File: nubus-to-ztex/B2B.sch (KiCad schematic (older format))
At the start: 17 parts, among them J1 Conn_02x07_Odd_Even, J3 Conn_01x06_Male

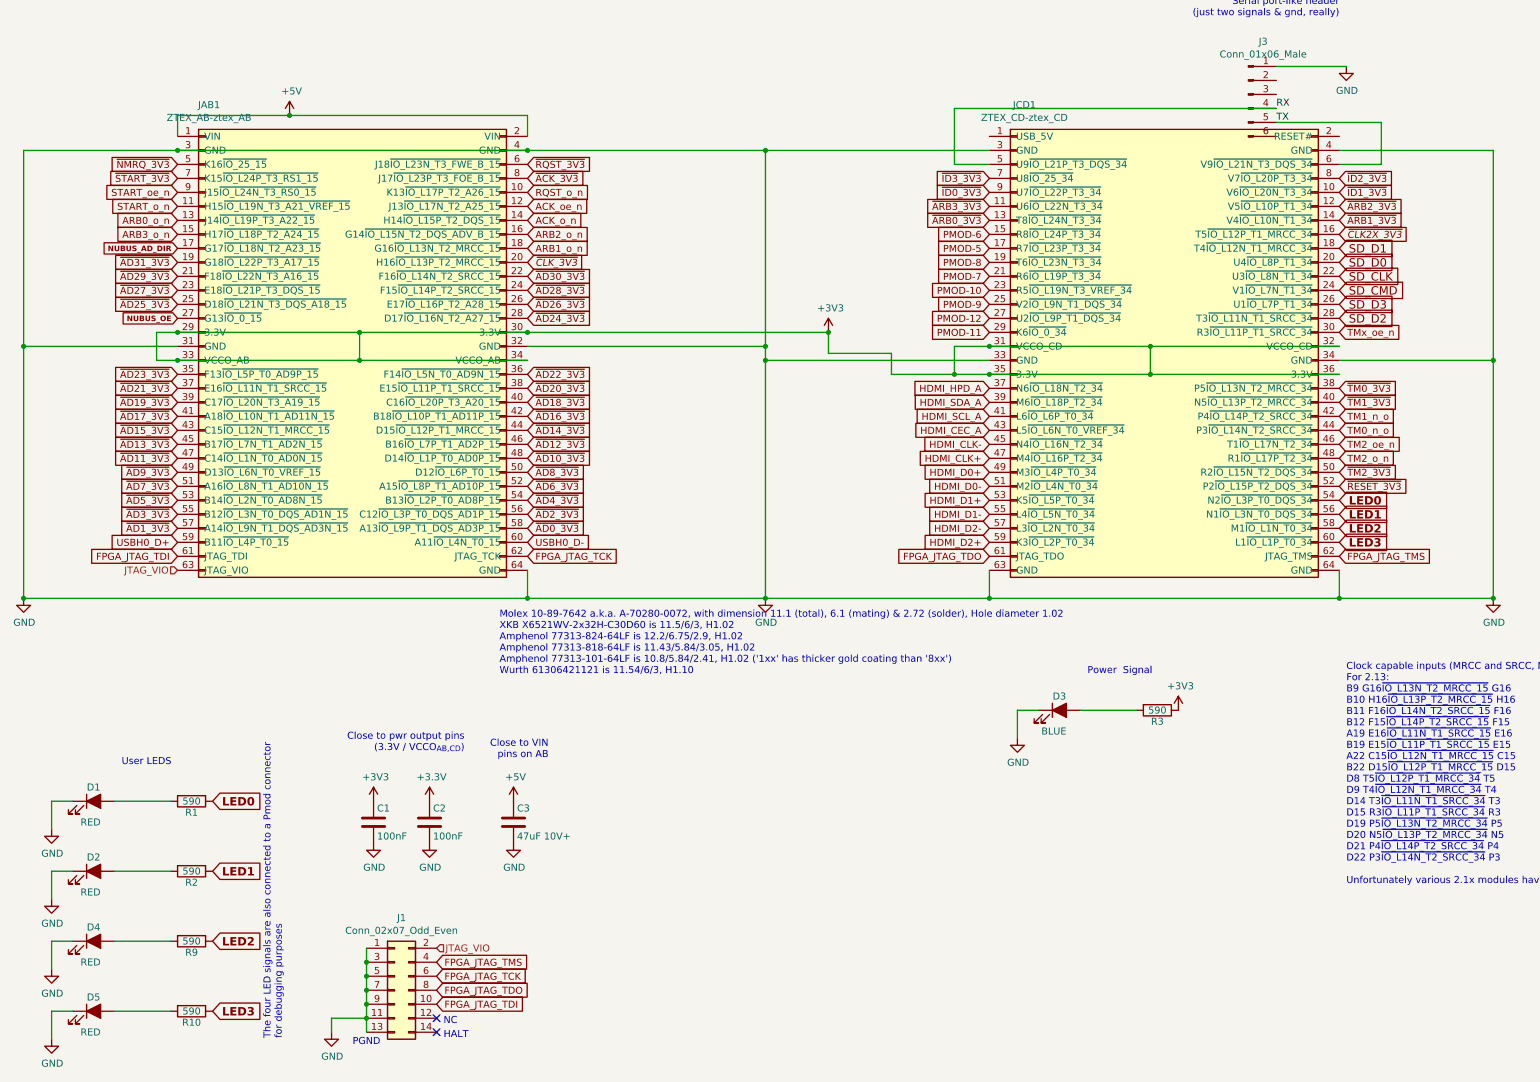
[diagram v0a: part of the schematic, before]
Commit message: merge pmod & leds into an extended pmod on the outside. Also some BoM updates.
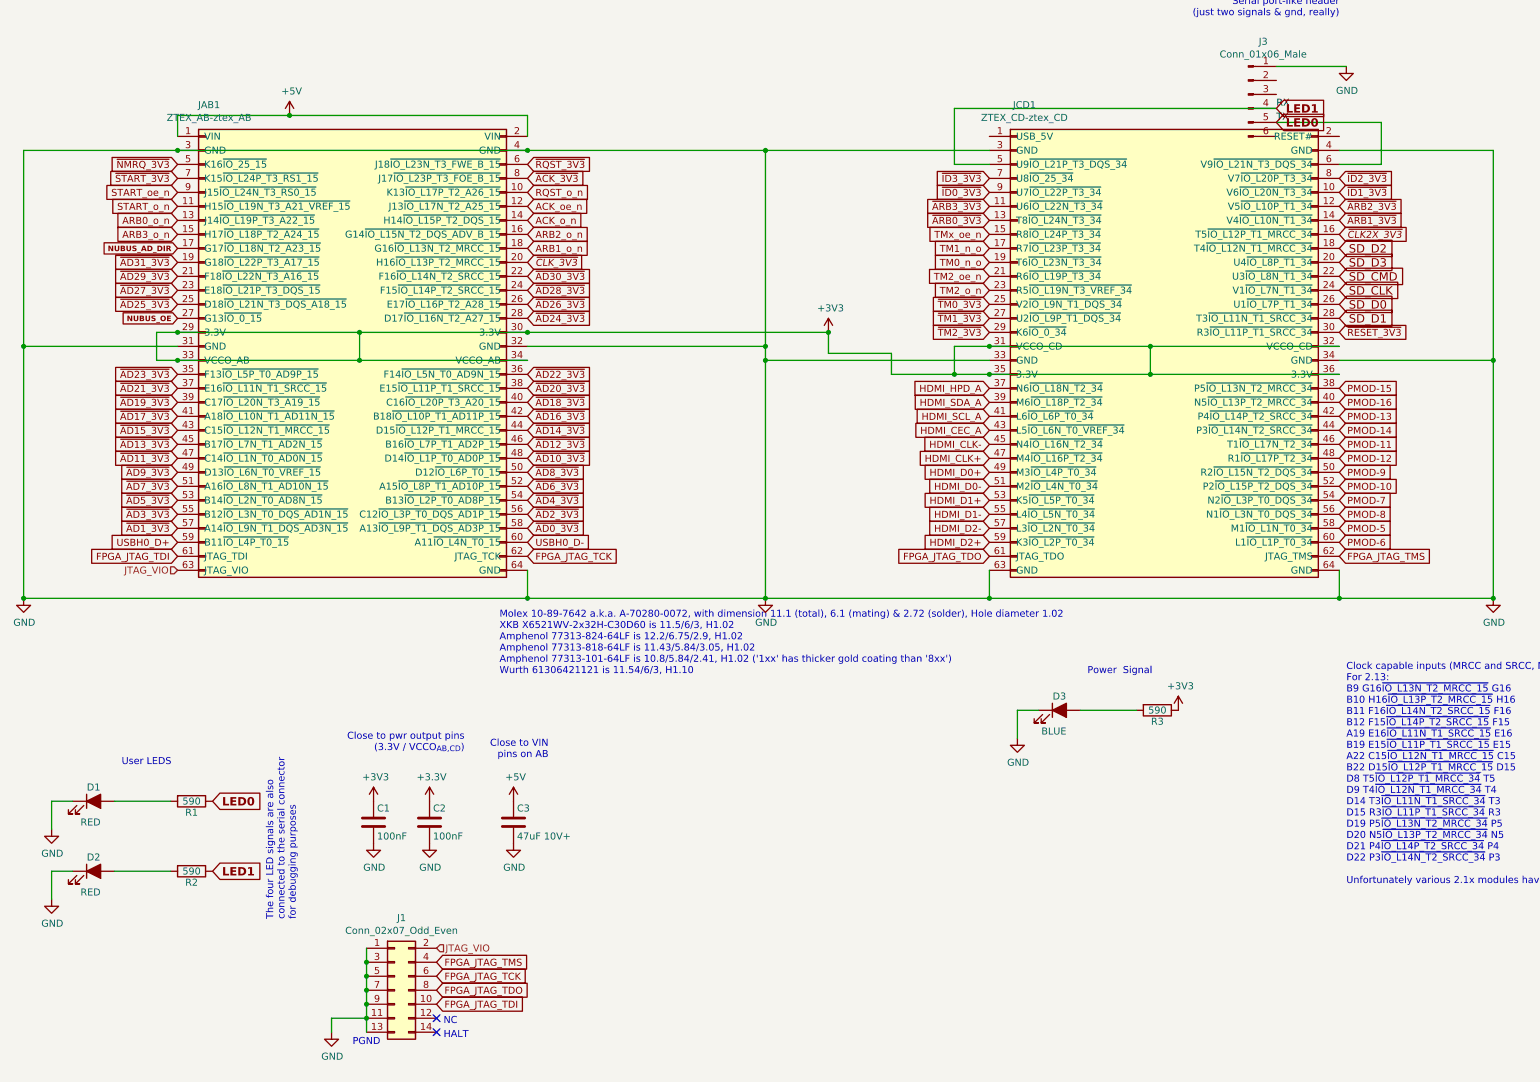
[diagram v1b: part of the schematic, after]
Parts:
- removed D4, D5: RED, LED_SMD:LED_0805_2012Metric, symbol Device:LED_ALT
- removed R10, R9: 590, Resistor_SMD:R_0603_1608Metric, symbol Device:R
- C2: URL (none) -> https://lcsc.com/product-detail/Multilayer-Ceramic-Capacito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
- C3: MPN C2012X5R1A476MTJ00E -> GRM21BR61A476ME15K; MPN-ALT (none) -> C2012X5R1A476MTJ00E; URL https://lcsc.com/product-detail/Multilayer-Ceramic-Capacito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 -> https://www.lcsc.com/product-detail/Multilayer-Ceramic-Capa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; URL-ALT (none) -> https://lcsc.com/product-detail/Multilayer-Ceramic-Capacito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
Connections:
- net LED2 is gone; now on net PMOD-5: JCD1.58 (M1~IO_L1N_T0_34)
- net LED3 is gone; now on net PMOD-6: JCD1.60 (L1~IO_L1P_T0_34)
- net RX is gone; now on net LED1: J3.4 (Pin_4), JCD1.5 (U9~IO_L21P_T3_DQS_34)
- net TX is gone; now on net LED0: J3.5 (Pin_5), JCD1.6 (V9~IO_L21N_T3_DQS_34)
- net LED0: no longer JCD1.54 (N2~IO_L3P_T0_DQS_34)
- net LED1: no longer JCD1.56 (N1~IO_L3N_T0_DQS_34)
- net PMOD-10: now also JCD1.52 (P2~IO_L15P_T2_DQS_34); no longer JCD1.23 (R5~IO_L19N_T3_VREF_34)
- net PMOD-11: now also JCD1.46 (T1~IO_L17N_T2_34); no longer JCD1.29 (K6~IO_0_34)
- net PMOD-12: now also JCD1.48 (R1~IO_L17P_T2_34); no longer JCD1.27 (U2~IO_L9P_T1_DQS_34)
- net PMOD-5: no longer JCD1.17 (R7~IO_L23P_T3_34)
- net PMOD-6: no longer JCD1.15 (R8~IO_L24P_T3_34)
- net PMOD-7: now also JCD1.54 (N2~IO_L3P_T0_DQS_34); no longer JCD1.21 (R6~IO_L19P_T3_34)
- net PMOD-8: now also JCD1.56 (N1~IO_L3N_T0_DQS_34); no longer JCD1.19 (T6~IO_L23N_T3_34)
- net PMOD-9: now also JCD1.50 (R2~IO_L15N_T2_DQS_34); no longer JCD1.25 (V2~IO_L9N_T1_DQS_34)
- net SD_CLK: now also JCD1.24 (V1~IO_L7N_T1_34); no longer JCD1.22 (U3~IO_L8N_T1_34)
- net SD_CMD: now also JCD1.22 (U3~IO_L8N_T1_34); no longer JCD1.24 (V1~IO_L7N_T1_34)
- net SD_D0: now also JCD1.26 (U1~IO_L7P_T1_34); no longer JCD1.20 (U4~IO_L8P_T1_34)
- net SD_D1: now also JCD1.28 (T3~IO_L11N_T1_SRCC_34); no longer JCD1.18 (T4~IO_L12N_T1_MRCC_34)
- net SD_D2: now also JCD1.18 (T4~IO_L12N_T1_MRCC_34); no longer JCD1.28 (T3~IO_L11N_T1_SRCC_34)
- net SD_D3: now also JCD1.20 (U4~IO_L8P_T1_34); no longer JCD1.26 (U1~IO_L7P_T1_34)
- net TM0_n_o: now also JCD1.19 (T6~IO_L23N_T3_34); no longer JCD1.44 (P3~IO_L14N_T2_SRCC_34)
- net TM1_n_o: now also JCD1.17 (R7~IO_L23P_T3_34); no longer JCD1.42 (P4~IO_L14P_T2_SRCC_34)
- net TM2_o_n: now also JCD1.23 (R5~IO_L19N_T3_VREF_34); no longer JCD1.48 (R1~IO_L17P_T2_34)
- net TM2_oe_n: now also JCD1.21 (R6~IO_L19P_T3_34); no longer JCD1.46 (T1~IO_L17N_T2_34)
- net TMx_oe_n: now also JCD1.15 (R8~IO_L24P_T3_34); no longer JCD1.30 (R3~IO_L11P_T1_SRCC_34)
- net ~RESET_3V3: now also JCD1.30 (R3~IO_L11P_T1_SRCC_34); no longer JCD1.52 (P2~IO_L15P_T2_DQS_34)
- net ~TM0_3V3: now also JCD1.25 (V2~IO_L9N_T1_DQS_34); no longer JCD1.38 (P5~IO_L13N_T2_MRCC_34)
- net ~TM1_3V3: now also JCD1.27 (U2~IO_L9P_T1_DQS_34); no longer JCD1.40 (N5~IO_L13P_T2_MRCC_34)
- net ~TM2_3V3: now also JCD1.29 (K6~IO_0_34); no longer JCD1.50 (R2~IO_L15N_T2_DQS_34)
- new net PMOD-13: JCD1.42 (P4~IO_L14P_T2_SRCC_34)
- new net PMOD-14: JCD1.44 (P3~IO_L14N_T2_SRCC_34)
- new net PMOD-15: JCD1.38 (P5~IO_L13N_T2_MRCC_34)
- new net PMOD-16: JCD1.40 (N5~IO_L13P_T2_MRCC_34)
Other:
- note added: "The four LED signals are also\nconnected to the serial connector\nfor debugging purposes"
- note removed: "The four LED signals are also connected to a Pmod connector\nfor debugging purposes"
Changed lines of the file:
@@
 $Descr A4 11693 8268
 encoding utf-8
-Sheet 2 10
+Sheet 2 9
 Title "nubus-to-ztex B2B connector"
 Date ""
@@
 	1    0    0    -1
 $EndComp
-Connection ~ 6250 2550
 Wire Wire Line
 	11000 2750 11000 4450
@@
 Text GLabel 4100 2150 2    50   Input ~ 0
 ~AD30_3V3
-Text GLabel 9900 3650 2    50   Input ~ 0
+Text GLabel 9900 2550 2    50   Input ~ 0
 ~RESET_3V3
-Text GLabel 9900 3050 2    50   Input ~ 0
+Text GLabel 7400 2450 0    50   Input ~ 0
 ~TM1_3V3
-Text GLabel 9900 2950 2    50   Input ~ 0
+Text GLabel 7400 2350 0    50   Input ~ 0
 ~TM0_3V3
 Text GLabel 1600 3950 0    50   Input ~ 0
@@
 Text GLabel 1850 6400 2    60   Input ~ 12
 LED1
-Text GLabel 9900 3750 2    60   Input ~ 12
+Text GLabel 9450 1050 2    60   Input ~ 12
 LED0
-Text GLabel 9900 3850 2    60   Input ~ 12
+Text GLabel 9450 950  2    60   Input ~ 12
 LED1
 Text GLabel 1600 4050 0    50   Input ~ 0
@@
 F 9 "?" H 3400 6050 50  0001 C CNN "Koncar"
 F 10 "TB" H 3400 6050 50  0001 C CNN "Side"
+F 11 "https://lcsc.com/product-detail/Multilayer-Ceramic-Capacitors-MLCC-SMD-SMT_YAGEO-CC0603KRX7R8BB104_C92490.html" H 3400 6050 50  0001 C CNN "URL"
 	1    3400 6050
 	1    0    0    -1
@@
 Text GLabel 1600 1350 0    50   Input ~ 0
 ~NMRQ_3V3
-Text GLabel 9900 3550 2    50   Input ~ 0
+Text GLabel 7400 2550 0    50   Input ~ 0
 ~TM2_3V3
 Text GLabel 9900 1850 2    50   Input Italic 0
@@
 F 2 "Capacitor_SMD:C_0805_2012Metric" H 4038 5900 50  0001 C CNN
 F 3 "" H 4000 6050 50  0000 C CNN
-F 4 "C2012X5R1A476MTJ00E" H 4000 6050 50  0001 C CNN "MPN"
-F 5 "https://lcsc.com/product-detail/Multilayer-Ceramic-Capacitors-MLCC-SMD-SMT_TDK-C2012X5R1A476MTJ00E_C76636.html" H 4000 6050 50  0001 C CNN "URL"
+F 4 "C2012X5R1A476MTJ00E" H 4000 6050 50  0001 C CNN "MPN-ALT"
+F 5 "https://lcsc.com/product-detail/Multilayer-Ceramic-Capacitors-MLCC-SMD-SMT_TDK-C2012X5R1A476MTJ00E_C76636.html" H 4000 6050 50  0001 C CNN "URL-ALT"
+F 6 "GRM21BR61A476ME15K" H 4000 6050 50  0001 C CNN "MPN"
+F 7 "https://www.lcsc.com/product-detail/Multilayer-Ceramic-Capacitors-MLCC-SMD-SMT_Murata-Electronics-GRM21BR61A476ME15K_C2292827.html" H 4000 6050 50  0001 C CNN "URL"
 	1    4000 6050
 	1    0    0    -1
@@
 Text GLabel 1600 1550 0    50   Input ~ 0
 START_oe_n
-Text GLabel 9900 2550 2    50   Input ~ 0
+Text GLabel 7400 1850 0    50   Input ~ 0
 TMx_oe_n
-Text GLabel 9900 3150 2    50   Input ~ 0
+Text GLabel 7400 1950 0    50   Input ~ 0
 TM1_n_o
-Text GLabel 9900 3250 2    50   Input ~ 0
+Text GLabel 7400 2050 0    50   Input ~ 0
 TM0_n_o
+Text GLabel 7400 2150 0    50   Input ~ 0
+TM2_oe_n
+Text GLabel 7400 2250 0    50   Input ~ 0
+TM2_o_n
+Text GLabel 9900 1950 2    60   Input ~ 0
+SD_D2
+Text GLabel 9900 2050 2    60   Input ~ 0
+SD_D3
+Text GLabel 9900 2150 2    60   Input ~ 0
+SD_CMD
+Text GLabel 9900 2250 2    60   Input ~ 0
+SD_CLK
+Text GLabel 9900 2350 2    60   Input ~ 0
+SD_D0
+Text GLabel 9900 2450 2    60   Input ~ 0
+SD_D1
+Text GLabel 9900 3950 2    50   Input ~ 0
+PMOD-5
+Text GLabel 9900 3750 2    50   Input ~ 0
+PMOD-7
+Text GLabel 9900 3550 2    50   Input ~ 0
+PMOD-9
 Text GLabel 9900 3350 2    50   Input ~ 0
-TM2_oe_n
+PMOD-11
 Text GLabel 9900 3450 2    50   Input ~ 0
-TM2_o_n
-Text GLabel 9900 2450 2    60   Input ~ 0
-SD_D2
-Text GLabel 9900 2350 2    60   Input ~ 0
-SD_D3
-Text GLabel 9900 2250 2    60   Input ~ 0
-SD_CMD
-Text GLabel 9900 2150 2    60   Input ~ 0
-SD_CLK
-Text GLabel 9900 2050 2    60   Input ~ 0
-SD_D0
-Text GLabel 9900 1950 2    60   Input ~ 0
-SD_D1
-Text GLabel 7400 1950 0    50   Input ~ 0
-PMOD-5
-Text GLabel 7400 2150 0    50   Input ~ 0
-PMOD-7
-Text GLabel 7400 2350 0    50   Input ~ 0
-PMOD-9
-Text GLabel 7400 2550 0    50   Input ~ 0
-PMOD-11
-Text GLabel 7400 2450 0    50   Input ~ 0
 PMOD-12
-Text GLabel 7400 1850 0    50   Input ~ 0
+Text GLabel 9900 4050 2    50   Input ~ 0
 PMOD-6
-Text GLabel 7400 2050 0    50   Input ~ 0
+Text GLabel 9900 3850 2    50   Input ~ 0
 PMOD-8
-Text GLabel 7400 2250 0    50   Input ~ 0
+Text GLabel 9900 3650 2    50   Input ~ 0
 PMOD-10
-Wire Wire Line
-	850  6900 700  6900
-Wire Wire Line
-	700  6900 700  7100
-Wire Wire Line
-	1150 6900 1550 6900
-$Comp
-L Device:R R?
-U 1 1 62CD698B
-P 1700 6900
-AR Path="/5F6B165A/62CD698B" Ref="R?"  Part="1"
-AR Path="/5F67E4B9/62CD698B" Ref="R?"  Part="1"
-AR Path="/618E8C75/62CD698B" Ref="R9"  Part="1"
-F 0 "R9" V 1780 6900 50  0000 C CNN
-F 1 "590" V 1700 6900 50  0000 C CNN
-F 2 "Resistor_SMD:R_0603_1608Metric" V 1630 6900 50  0001 C CNN
-F 3 "" H 1700 6900 50  0000 C CNN
-F 4 "0603WAF5900T5E" V 1700 6900 50  0001 C CNN "MPN"
-F 5 "https://www.lcsc.com/product-detail/Chip-Resistor-Surface-Mount_UNI-ROYAL-Uniroyal-Elec-0603WAF5900T5E_C23084.html" V 1700 6900 50  0001 C CNN "URL"
-	1    1700 6900
-	0    1    1    0
-$EndComp
-$Comp
-L Device:LED_ALT D?
-U 1 1 62CD6995
-P 1000 6900
-AR Path="/5F6B165A/62CD6995" Ref="D?"  Part="1"
-AR Path="/5F67E4B9/62CD6995" Ref="D?"  Part="1"
-AR Path="/618E8C75/62CD6995" Ref="D4"  Part="1"
-F 0 "D4" H 1000 7000 50  0000 C CNN
-F 1 "RED" H 1050 6750 50  0000 R CNN
-F 2 "LED_SMD:LED_0805_2012Metric" H 1000 6900 50  0001 C CNN
-F 3 "https://optoelectronics.liteon.com/upload/download/DS-22-99-0150/LTST-C170KRKT.pdf" H 1000 6900 50  0001 C CNN
-F 4 "www.liteon.com" H 1000 6900 60  0001 C CNN "MNF1_URL"
-F 5 "LTST-C170KRKT" H 1000 6900 60  0001 C CNN "MPN"
-F 6 "https://www.lcsc.com/product-detail/Light-Emitting-Diodes-LED_Lite-On-LTST-C170KRKT_C94868.html" H 1000 6900 50  0001 C CNN "URL"
-	1    1000 6900
-	1    0    0    -1
-$EndComp
-$Comp
-L power:GND #PWR0142
-U 1 1 62CD699C
-P 700 7100
-F 0 "#PWR0142" H 700 6850 50  0001 C CNN
-F 1 "GND" H 705 6927 50  0000 C CNN
-F 2 "" H 700 7100 50  0001 C CNN
-F 3 "" H 700 7100 50  0001 C CNN
-	1    700  7100
-	1    0    0    -1
-$EndComp
-Text GLabel 1850 6900 2    60   Input ~ 12
-LED2
-Wire Wire Line
-	850  7400 700  7400
-Wire Wire Line
-	700  7400 700  7600
-Wire Wire Line
-	1150 7400 1550 7400
-$Comp
-L Device:R R?
-U 1 1 62CD69A8
-P 1700 7400
-AR Path="/5F6B165A/62CD69A8" Ref="R?"  Part="1"
-AR Path="/5F67E4B9/62CD69A8" Ref="R?"  Part="1"
-AR Path="/618E8C75/62CD69A8" Ref="R10"  Part="1"
-F 0 "R10" V 1780 7400 50  0000 C CNN
-F 1 "590" V 1700 7400 50  0000 C CNN
-F 2 "Resistor_SMD:R_0603_1608Metric" V 1630 7400 50  0001 C CNN
-F 3 "" H 1700 7400 50  0000 C CNN
-F 4 "0603WAF5900T5E" V 1700 7400 50  0001 C CNN "MPN"
-F 5 "https://www.lcsc.com/product-detail/Chip-Resistor-Surface-Mount_UNI-ROYAL-Uniroyal-Elec-0603WAF5900T5E_C23084.html" V 1700 7400 50  0001 C CNN "URL"
-	1    1700 7400
-	0    1    1    0
-$EndComp
-$Comp
-L Device:LED_ALT D?
-U 1 1 62CD69B2
-P 1000 7400
-AR Path="/5F6B165A/62CD69B2" Ref="D?"  Part="1"
-AR Path="/5F67E4B9/62CD69B2" Ref="D?"  Part="1"
-AR Path="/618E8C75/62CD69B2" Ref="D5"  Part="1"
-F 0 "D5" H 1000 7500 50  0000 C CNN
-F 1 "RED" H 1050 7250 50  0000 R CNN
-F 2 "LED_SMD:LED_0805_2012Metric" H 1000 7400 50  0001 C CNN
-F 3 "https://optoelectronics.liteon.com/upload/download/DS-22-99-0150/LTST-C170KRKT.pdf" H 1000 7400 50  0001 C CNN
-F 4 "www.liteon.com" H 1000 7400 60  0001 C CNN "MNF1_URL"
-F 5 "LTST-C170KRKT" H 1000 7400 60  0001 C CNN "MPN"
-F 6 "https://www.lcsc.com/product-detail/Light-Emitting-Diodes-LED_Lite-On-LTST-C170KRKT_C94868.html" H 1000 7400 50  0001 C CNN "URL"
-	1    1000 7400
-	1    0    0    -1
-$EndComp
-$Comp
-L power:GND #PWR0143
-U 1 1 62CD69B9
-P 700 7600
-F 0 "#PWR0143" H 700 7350 50  0001 C CNN
-F 1 "GND" H 705 7427 50  0000 C CNN
-F 2 "" H 700 7600 50  0001 C CNN
-F 3 "" H 700 7600 50  0001 C CNN
-	1    700  7600
-	1    0    0    -1
-$EndComp
-Text GLabel 1850 7400 2    60   Input ~ 12
-LED3
-Text GLabel 9900 3950 2    60   Input ~ 12
-LED2
-Text GLabel 9900 4050 2    60   Input ~ 12
-LED3
 Text Notes 3900 5000 0    50   ~ 0
 Molex 10-89-7642 a.k.a. A-70280-0072, with dimension 11.1 (total), 6.1 (mating) & 2.72 (solder), Hole diameter 1.02\nXKB X6521WV-2x32H-C30D60 is 11.5/6/3, H1.02\nAmphenol 77313-824-64LF is 12.2/6.75/2.9, H1.02\nAmphenol 77313-818-64LF is 11.43/5.84/3.05, H1.02\nAmphenol 77313-101-64LF is 10.8/5.84/2.41, H1.02 ('1xx' has thicker gold coating than '8xx')\nWurth 61306421121 is 11.54/6/3, H1.10\n
-Text Notes 2350 7600 1    50   ~ 0
-The four LED signals are also connected to a Pmod connector\nfor debugging purposes
+Text Notes 2450 6750 1    50   ~ 0
+The four LED signals are also\nconnected to the serial connector\nfor debugging purposes
+Connection ~ 6250 2550
+Text GLabel 9900 3250 2    50   Input ~ 0
+PMOD-14
+Text GLabel 9900 3150 2    50   Input ~ 0
+PMOD-13
+Text GLabel 9900 3050 2    50   Input ~ 0
+PMOD-16
+Text GLabel 9900 2950 2    50   Input ~ 0
+PMOD-15
 $EndSCHEMATC
